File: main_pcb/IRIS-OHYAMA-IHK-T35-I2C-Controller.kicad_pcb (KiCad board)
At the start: 2 copper layers, 255 x 35 mm, 58 parts, among them CN1 Conn_01x05, J1 Grove, J2 Conn_01x06, J3 thermistor, Q1 Q_NMOS_DGS, Q2 Q_NMOS_DGS, Q3 Q_NMOS_DGS, Q4 Q_NMOS_DGS, U1 74HC164, U2 ATmega328P-MU

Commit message: Put footprints in 203.5x35mm
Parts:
- moved CN1 51.5 mm to (197.5, 59.7)
- moved D13 51.5 mm to (187.6, 64.5)
- moved D14 51.5 mm to (165.8, 63.9)
- moved D7 51.5 mm to (206.5, 64.5)
- moved D8 51.5 mm to (176.5, 64.5)
- moved J1 51.5 mm to (168.8, 58.9)
- moved J3 51.5 mm to (158.6, 60.0)
- moved KEY1 51.5 mm to (206.5, 73.5)
- moved KEY2 51.5 mm to (148.5, 73.5)
- moved KEY3 51.5 mm to (124.5, 73.5)
- moved KEY5 51.5 mm to (176.5, 73.5)
- moved R10 51.5 mm to (143.0, 73.5)
- moved R11 51.5 mm to (119.0, 73.6)
- moved R13 51.5 mm to (171.1, 73.6)
- moved R7 51.5 mm to (206.5, 66.0)
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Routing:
- net GND: track 364.8 -> 478.1 mm, vias 16 -> 19
- net /A1: track 215.8 -> 165.7 mm, vias 3 -> 2
- net /D10: track 202.4 -> 161.6 mm
- net /D4: track 217.8 -> 177.2 mm, vias 2 -> 0
- net /CLK: track 159.7 -> 121.0 mm, vias 0 -> 2
- net /A3: track 109.2 -> 71.6 mm
- net /D8: track 35.5 -> 65.4 mm, vias 2 -> 0
- net /A0: track 249.8 -> 221.4 mm, vias 2 -> 4
- net /D6: track 41.0 -> 68.0 mm
- net /D5: track 47.5 -> 71.4 mm
- net /Controller_5V: track 153.7 -> 129.7 mm, vias 0 -> 3
- net /A6: track 97.7 -> 75.4 mm, vias 0 -> 1
- net /SDA: track 110.3 -> 88.3 mm
- net /SCL: track 108.4 -> 86.4 mm
- net /D7: track 31.0 -> 51.9 mm, vias 2 -> 0
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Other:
- board size 255 x 35 mm -> 203.5 x 35 mm

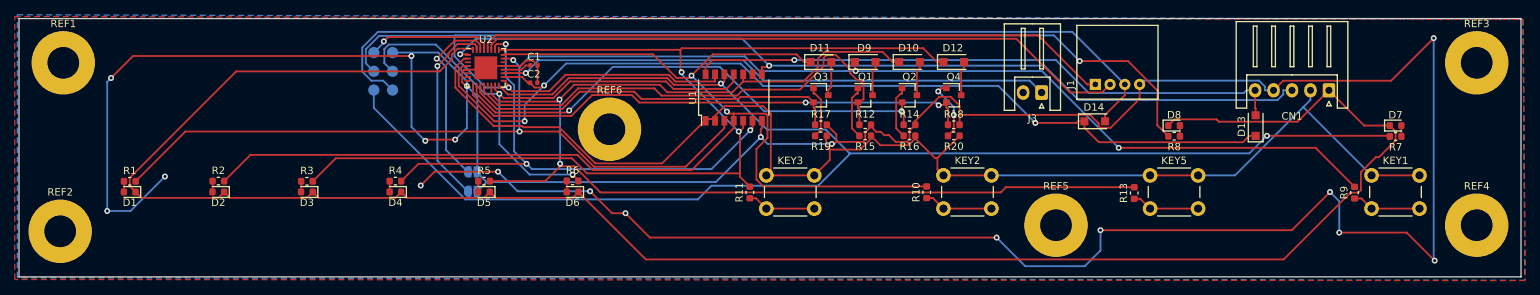
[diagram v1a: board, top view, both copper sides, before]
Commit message: Change outline to 199.5x35mm
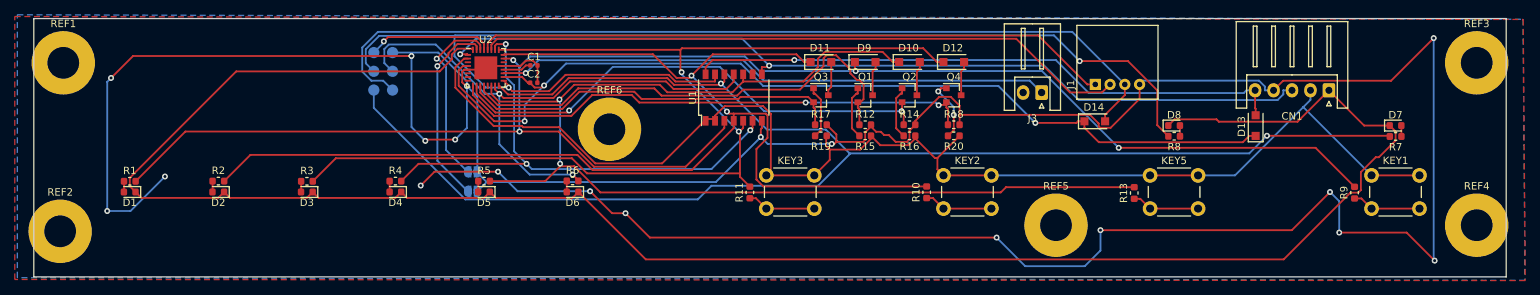
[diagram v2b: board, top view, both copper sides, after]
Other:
- board size 203.5 x 35 mm -> 199.5 x 35 mm

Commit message: Update silk info
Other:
- board text added: "Rev2020.05"
- board text removed: "Rev2020.04"
